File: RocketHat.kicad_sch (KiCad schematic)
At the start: 28 parts, among them J1 Conn_01x06_Female, J10 Conn_01x10_Female, J11 Raspberry_Pi_2_3, J2 Conn_01x06_Female, J3 Conn_01x07_Female, J4 Conn_01x06_Female, J5 Conn_01x04_Female, J6 Conn_01x02_Female, J7 Conn_01x02, J8 Conn_01x10_Female, J9 Conn_01x02, Q1 2N3904, Q2 DMG2305UX-13, Q3 2N3904, U1 CAT24C128

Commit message: Fixed All DRC Errors
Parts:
- R1: footprint Resistor_SMD:R_0603_1608Metric_Pad0.98x0.95mm_HandSolder -> Resistor_SMD:R_0603_1608Metric
- R2, R3, R4, R5, R6: footprint Resistor_SMD:R_0201_0603Metric -> Resistor_SMD:R_0603_1608Metric
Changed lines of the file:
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@@
     (property "Reference" "R3" (id 0) (at 83.82 147.32 90))
     (property "Value" "10K" (id 1) (at 83.82 149.86 90))
-    (property "Footprint" "Resistor_SMD:R_0201_0603Metric" (id 2) (at 83.82 149.86 0)
+    (property "Footprint" "Resistor_SMD:R_0603_1608Metric" (id 2) (at 83.82 149.86 0)
       (effects (font (size 1.27 1.27)) hide)
     )
@@
       (effects (font (size 1.27 1.27)) (justify left))
     )
-    (property "Footprint" "Resistor_SMD:R_0201_0603Metric" (id 2) (at 166.37 31.75 0)
+    (property "Footprint" "Resistor_SMD:R_0603_1608Metric" (id 2) (at 166.37 31.75 0)
       (effects (font (size 1.27 1.27)) hide)
     )
@@
       (effects (font (size 1.27 1.27)) (justify left))
     )
-    (property "Footprint" "Resistor_SMD:R_0201_0603Metric" (id 2) (at 179.705 31.75 0)
+    (property "Footprint" "Resistor_SMD:R_0603_1608Metric" (id 2) (at 179.705 31.75 0)
       (effects (font (size 1.27 1.27)) hide)
     )
@@
       (effects (font (size 1.27 1.27)) (justify left))
     )
-    (property "Footprint" "Resistor_SMD:R_0201_0603Metric" (id 2) (at 69.85 59.69 0)
+    (property "Footprint" "Resistor_SMD:R_0603_1608Metric" (id 2) (at 69.85 59.69 0)
       (effects (font (size 1.27 1.27)) hide)
     )
@@
     (property "Reference" "R4" (id 0) (at 163.83 43.18 90))
     (property "Value" "10K 1%" (id 1) (at 163.83 45.72 90))
-    (property "Footprint" "Resistor_SMD:R_0201_0603Metric" (id 2) (at 162.56 48.26 0)
+    (property "Footprint" "Resistor_SMD:R_0603_1608Metric" (id 2) (at 162.56 48.26 0)
       (effects (font (size 1.27 1.27)) hide)
     )
@@
       (effects (font (size 1.27 1.27)) (justify left))
     )
-    (property "Footprint" "Resistor_SMD:R_0603_1608Metric_Pad0.98x0.95mm_HandSolder" (id 2) (at 48.26 59.69 0)
+    (property "Footprint" "Resistor_SMD:R_0603_1608Metric" (id 2) (at 48.26 59.69 0)
       (effects (font (size 1.27 1.27)) hide)
     )
@@
     )
     (path "/ca730761-fedf-4eae-98fa-a8325d785a83"
-      (reference "R1") (unit 1) (value "10K") (footprint "Resistor_SMD:R_0603_1608Metric_Pad0.98x0.95mm_HandSolder")
+      (reference "R1") (unit 1) (value "10K") (footprint "Resistor_SMD:R_0603_1608Metric")
     )
     (path "/99482937-6b39-4a5d-873b-9c8df7ef1a29"
-      (reference "R2") (unit 1) (value "47K") (footprint "Resistor_SMD:R_0201_0603Metric")
+      (reference "R2") (unit 1) (value "47K") (footprint "Resistor_SMD:R_0603_1608Metric")
     )
     (path "/371e2c35-1dd3-4ab9-a165-5756dbc0abde"
-      (reference "R3") (unit 1) (value "10K") (footprint "Resistor_SMD:R_0201_0603Metric")
+      (reference "R3") (unit 1) (value "10K") (footprint "Resistor_SMD:R_0603_1608Metric")
     )
     (path "/b3a76419-7e89-43a3-815b-bdb71a4ebfe5"
-      (reference "R4") (unit 1) (value "10K 1%") (footprint "Resistor_SMD:R_0201_0603Metric")
+      (reference "R4") (unit 1) (value "10K 1%") (footprint "Resistor_SMD:R_0603_1608Metric")
     )
     (path "/483c471a-9441-4eae-bda1-202ac6c7fbd5"
-      (reference "R5") (unit 1) (value "3.9K") (footprint "Resistor_SMD:R_0201_0603Metric")
+      (reference "R5") (unit 1) (value "3.9K") (footprint "Resistor_SMD:R_0603_1608Metric")
     )
     (path "/606feb5f-e625-4acf-b51e-f13172bce11b"
-      (reference "R6") (unit 1) (value "3.9K") (footprint "Resistor_SMD:R_0201_0603Metric")
+      (reference "R6") (unit 1) (value "3.9K") (footprint "Resistor_SMD:R_0603_1608Metric")
     )
     (path "/7e172c4b-1dda-4e37-981f-3dc1a6417140"

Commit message: Set Mounting Holes 1&2 to M2
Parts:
- H1, H2: footprint MountingHole:MountingHole_2.1mm -> MountingHole:MountingHole_2.2mm_M2
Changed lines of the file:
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@@
       (effects (font (size 1.27 1.27)) (justify left))
     )
-    (property "Footprint" "MountingHole:MountingHole_2.1mm" (id 2) (at 91.44 176.53 0)
+    (property "Footprint" "MountingHole:MountingHole_2.2mm_M2" (id 2) (at 91.44 176.53 0)
       (effects (font (size 1.27 1.27)) hide)
     )
@@
       (effects (font (size 1.27 1.27)) (justify left))
     )
-    (property "Footprint" "MountingHole:MountingHole_2.1mm" (id 2) (at 72.39 176.53 0)
+    (property "Footprint" "MountingHole:MountingHole_2.2mm_M2" (id 2) (at 72.39 176.53 0)
       (effects (font (size 1.27 1.27)) hide)
     )
@@
     )
     (path "/9745344d-f5a4-4b56-b292-fac7f1ad12d0"
-      (reference "H1") (unit 1) (value "MountingHole") (footprint "MountingHole:MountingHole_2.1mm")
+      (reference "H1") (unit 1) (value "MountingHole") (footprint "MountingHole:MountingHole_2.2mm_M2")
     )
     (path "/8fae6204-f081-4a3a-877b-32ca9fce4a19"
-      (reference "H2") (unit 1) (value "MountingHole") (footprint "MountingHole:MountingHole_2.1mm")
+      (reference "H2") (unit 1) (value "MountingHole") (footprint "MountingHole:MountingHole_2.2mm_M2")
     )
     (path "/c69243ef-117d-41ea-9017-9b9ab8c0a016"

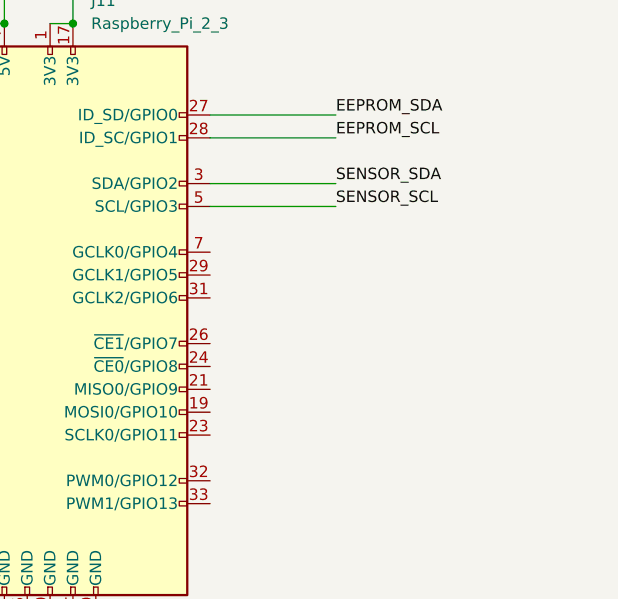
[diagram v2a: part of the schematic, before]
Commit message: Added Flood Zone
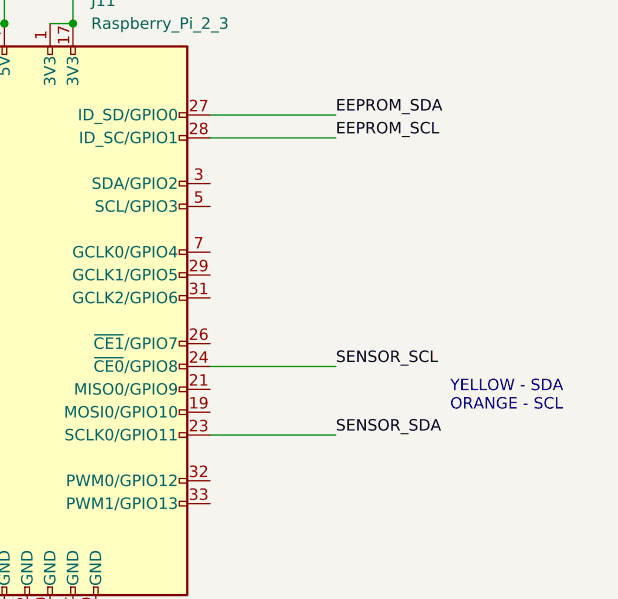
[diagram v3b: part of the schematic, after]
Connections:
- net SENSOR_SCL: now also J11.24 (~{CE0}/GPIO8); no longer J11.5 (SCL/GPIO3)
- net SENSOR_SDA: now also J11.23 (SCLK0/GPIO11); no longer J11.3 (SDA/GPIO2)
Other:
- note added: "YELLOW - SDA ORANGE - SCL"
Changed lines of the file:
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@@
+    (stroke (width 0) (type default) (color 0 0 0 0))
+  )
+  (wire (pts (xy 231.14 116.84) (xy 245.11 116.84))
     (stroke (width 0) (type default) (color 0 0 0 0))
   )
@@
     (stroke (width 0) (type default) (color 0 0 0 0))
   )
-  (wire (pts (xy 231.14 91.44) (xy 245.11 91.44))
-    (stroke (width 0) (type default) (color 0 0 0 0))
-  )
   (wire (pts (xy 87.63 143.51) (xy 91.44 143.51))
     (stroke (width 0) (type default) (color 0 0 0 0))
@@
     (stroke (width 0) (type default) (color 0 0 0 0))
   )
+  (wire (pts (xy 231.14 109.22) (xy 245.11 109.22))
+    (stroke (width 0) (type default) (color 0 0 0 0))
+  )
   (wire (pts (xy 166.37 26.67) (xy 166.37 29.21))
     (stroke (width 0) (type default) (color 0 0 0 0))
   )
-  (wire (pts (xy 231.14 88.9) (xy 245.11 88.9))
-    (stroke (width 0) (type default) (color 0 0 0 0))
-  )
   (polyline (pts (xy 33.02 160.02) (xy 107.95 160.02))
     (stroke (width 0) (type default) (color 0 0 0 0))
@@
   )
   (text "Jumper is for\nground-testing\npruposes only" (at 87.63 45.72 0)
+    (effects (font (size 1.27 1.27)) (justify left bottom))
+  )
+  (text "YELLOW - SDA\nORANGE - SCL\n" (at 257.81 114.3 0)
     (effects (font (size 1.27 1.27)) (justify left bottom))
   )
@@
     (effects (font (size 1.27 1.27)) (justify left bottom))
   )
-  (label "SENSOR_SDA" (at 245.11 88.9 0)
-    (effects (font (size 1.27 1.27)) (justify left bottom))
-  )
   (label "3V3" (at 166.37 48.26 0)
     (effects (font (size 1.27 1.27)) (justify left bottom))
   )
-  (label "SENSOR_SCL" (at 245.11 91.44 0)
-    (effects (font (size 1.27 1.27)) (justify left bottom))
-  )
   (label "P5V_HAT" (at 208.28 60.96 90)
     (effects (font (size 1.27 1.27)) (justify left bottom))
@@
     (effects (font (size 1.27 1.27)) (justify left bottom))
   )
+  (label "SENSOR_SCL" (at 245.11 109.22 0)
+    (effects (font (size 1.27 1.27)) (justify left bottom))
+  )
   (label "XBEE_TX" (at 129.54 116.84 180)
     (effects (font (size 1.27 1.27)) (justify right bottom))
@@
     (effects (font (size 1.27 1.27)) (justify left bottom))
   )
+  (label "SENSOR_SDA" (at 245.11 116.84 0)
+    (effects (font (size 1.27 1.27)) (justify left bottom))
+  )

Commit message: Version 1.1.0
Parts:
- removed J6: Conn_01x02_Female, Connector_Wago:Wago_734-162_1x02_P3.50mm_Horizontal, symbol Connector:Conn_01x02_Female
- removed J7: Conn_01x02, Connector_PinHeader_2.54mm:PinHeader_1x02_P2.54mm_Vertical, symbol Connector_Generic:Conn_01x02
- removed Q1, Q3: 2N3904, Package_TO_SOT_THT:TO-92_Inline, symbol Transistor_BJT:2N3904
- removed Q2: DMG2305UX-13, digikey-footprints:SOT-23-3, symbol dk_Transistors-FETs-MOSFETs-Single:DMG2305UX-13
- removed R1: 10K, Resistor_SMD:R_0603_1608Metric, symbol Device:R_Small
- removed R2: 47K, Resistor_SMD:R_0603_1608Metric, symbol Device:R_Small
- added J1: Screw_Terminal_01x02, TerminalBlock_Phoenix:TerminalBlock_Phoenix_MKDS-1,5-2_1x02_P5.00mm_Horizontal, symbol Connector:Screw_Terminal_01x02
- added Q1: FQP27P06, Package_TO_SOT_THT:TO-220-3_Vertical, symbol Transistor_FET:FQP27P06
- R2: renamed from R3; footprint Resistor_SMD:R_0603_1608Metric -> Resistor_THT:R_Axial_DIN0204_L3.6mm_D1.6mm_P5.08mm_Horizontal
- R3: renamed from R4; footprint Resistor_SMD:R_0603_1608Metric -> Resistor_THT:R_Axial_DIN0204_L3.6mm_D1.6mm_P5.08mm_Horizontal
- R4: renamed from R5; footprint Resistor_SMD:R_0603_1608Metric -> Resistor_THT:R_Axial_DIN0204_L3.6mm_D1.6mm_P5.08mm_Horizontal
- R5: renamed from R6; footprint Resistor_SMD:R_0603_1608Metric -> Resistor_THT:R_Axial_DIN0204_L3.6mm_D1.6mm_P5.08mm_Horizontal
- renumbered J11 to J10, J1 to J2, J2 to J3, J3 to J4, J4 to J5, J5 to J6, J8 to J7, J9 to J8, J10 to J9, JP1 to JP2
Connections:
- net 3V3: now also J5.6 (Pin_6)
- net GND: now also J1.2 (Pin_2), Q1.1 (G)
- net P5V_HAT: now also Q1.3 (S)
- new net: J1.1 (Pin_1), Q1.2 (D)
- no-connect marks 0 -> 53
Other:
- note added: "+5V"
- note added: "3V3O"
- note added: "CS"
- note added: "D"
- note added: "G"
- note added: "GND"
- note added: "I2"
- note added: "INT"
- note added: "INT1"
- note added: "INT2"
- note added: "NC"
- note added: "PS0"
- note added: "PS1"
- note added: "RST"
- note added: "Reverse Polarity Protection"
- note added: "S"
- note added: "SDO"
- note removed: "Backflow Power Protection"
- note removed: "Jumper is for ground-testing pruposes only"
- note removed: "Schematic Provided by Raspberry Pi Foundation https://github.com/raspberrypi/hats/blob/master/designguide.md"
- moved on the sheet: J10, J2, J5

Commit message: PCB Updates
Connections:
- net BNORST: now reaches J10.15 (GPIO22)
- net BNORST: now also J3.6 (Pin_6)
- no-connect marks 53 -> 51
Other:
- note removed: "RST"
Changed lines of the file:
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@@
   (no_connect (at 59.69 127))
   (no_connect (at 154.94 124.46))
-  (no_connect (at 59.69 137.16))
   (no_connect (at 76.2 71.12))
   (no_connect (at 76.2 73.66))
@@
   (no_connect (at 193.04 101.6))
   (no_connect (at 193.04 104.14))
-  (no_connect (at 193.04 109.22))
   (no_connect (at 193.04 111.76))
   (no_connect (at 193.04 114.3))
@@
     (stroke (width 0) (type default) (color 0 0 0 0))
   )
+  (wire (pts (xy 52.705 137.16) (xy 59.69 137.16))
+    (stroke (width 0) (type default) (color 0 0 0 0))
+  )
   (wire (pts (xy 50.8 168.91) (xy 60.96 168.91))
     (stroke (width 0) (type default) (color 0 0 0 0))
@@
   )
   (wire (pts (xy 50.8 38.1) (xy 62.23 38.1))
+    (stroke (width 0) (type default) (color 0 0 0 0))
+  )
+  (wire (pts (xy 188.595 109.22) (xy 193.04 109.22))
     (stroke (width 0) (type default) (color 0 0 0 0))
   )
@@
     (effects (font (size 1.27 1.27) (thickness 0.254) bold) (justify right bottom))
   )
-  (text "RST" (at 58.42 137.16 180)
-    (effects (font (size 1.27 1.27)) (justify right bottom))
-  )
   (text "3V3O" (at 59.055 127 180)
     (effects (font (size 1.27 1.27)) (justify right bottom))
@@
     (effects (font (size 1.27 1.27)) (justify right bottom))
   )
+  (label "BNORST" (at 52.705 137.16 180)
+    (effects (font (size 1.27 1.27)) (justify right bottom))
+  )
   (label "SENSOR_SCL" (at 52.07 132.08 180)
     (effects (font (size 1.27 1.27)) (justify right bottom))
@@
     (effects (font (size 1.27 1.27)) (justify right bottom))
   )
+  (label "BNORST" (at 188.595 109.22 180)
+    (effects (font (size 1.27 1.27)) (justify right bottom))
+  )

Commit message: Cool Thicc Lines
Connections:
- net BNORST: now also J10.18 (GPIO24); no longer J10.15 (GPIO22)
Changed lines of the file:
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@@
   (no_connect (at 134.62 132.08))
   (no_connect (at 134.62 124.46))
+  (no_connect (at 193.04 109.22))
   (no_connect (at 134.62 129.54))
   (no_connect (at 76.2 81.28))
@@
   (no_connect (at 193.04 104.14))
   (no_connect (at 193.04 111.76))
-  (no_connect (at 193.04 114.3))
   (no_connect (at 193.04 116.84))
   (no_connect (at 193.04 119.38))
@@
     (stroke (width 0) (type default) (color 0 0 0 0))
   )
+  (wire (pts (xy 188.595 114.3) (xy 193.04 114.3))
+    (stroke (width 0) (type default) (color 0 0 0 0))
+  )
   (polyline (pts (xy 189.23 19.05) (xy 189.23 60.96))
     (stroke (width 0) (type default) (color 0 0 0 0))
@@
   )
   (wire (pts (xy 50.8 38.1) (xy 62.23 38.1))
-    (stroke (width 0) (type default) (color 0 0 0 0))
-  )
-  (wire (pts (xy 188.595 109.22) (xy 193.04 109.22))
     (stroke (width 0) (type default) (color 0 0 0 0))
   )
@@
     (effects (font (size 1.27 1.27)) (justify right bottom))
   )
-  (label "BNORST" (at 188.595 109.22 180)
-    (effects (font (size 1.27 1.27)) (justify right bottom))
-  )
+  (label "BNORST" (at 188.595 114.3 180)
+    (effects (font (size 1.27 1.27)) (justify right bottom))
+  )
